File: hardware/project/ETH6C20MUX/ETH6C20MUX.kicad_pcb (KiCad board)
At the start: 4 copper layers, 160 x 100 mm, 197 parts, among them J301 5499141-4, J501 Conn_02x06_Odd_Even, J502 Conn_02x08_Odd_Even, J503 C64AC, J601 Conn_02x05, J602 Conn_02x01, K301 HE3621A0510, K302 HE3621A0510, K303 HE3621A0510, K304 HE3621A0510, K305 HE3621A0510, K306 HE3621A0510, K307 HE3621A0510, K308 HE3621A0510, K309 HE3621A0510, K310 HE3621A0510, K311 HE3621A0510, K312 HE3621A0510, K313 HE3621A0510, K314 HE3621A0510, K315 HE3621A0510, K316 HE3621A0510, K317 HE3621A0510, K318 HE3621A0510, K319 HE3621A0510, K320 HE3621A0510, K321 HE3621A0510, K322 HE3621A0510, K323 HE3621A0510, K324 HE3621A0510, K325 HE3621A0510, K326 HE3621A0510, K327 HE3621A0510, K328 HE3621A0510, K329 HE3621A0510, K330 HE3621A0510, K331 HE3621A0510, K332 HE3621A0510, K333 HE3621A0510, K334 HE3621A0510, K335 HE3621A0510, K336 HE3621A0510, K337 HE3621A0510, K338 HE3621A0510, K339 HE3621A0510, K340 HE3621A0510, K341 HE3621A0510, K342 HE3621A0510, K343 HE3621A0510, K344 HE3621A0510, K345 HE3621A0510, K346 HE3621A0510, K347 HE3621A0510, K348 HE3621A0510, K349 HE3621A0510, K350 HE3621A0510, K351 HE3621A0510, K352 HE3621A0510, K353 HE3621A0510, K354 HE3621A0510, K355 HE3621A0510, K356 HE3621A0510, K357 HE3621A0510, K358 HE3621A0510, K359 HE3621A0510, K360 HE3621A0510, K361 HE3621A0510, K362 HE3621A0510, K363 HE3621A0510, K364 HE3621A0510, K365 HE3621A0510, K366 HE3621A0510, K367 HE3621A0510, K368 HE3621A0510, K369 HE3621A0510, K370 HE3621A0510, Q401 IRFR5410, SW601 A6SN-5104, U201 LC03-3.3, U202 LAN8742A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

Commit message: Modifications in PCB main board.
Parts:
- moved R401 0.76 mm to (205.0, 132.7)
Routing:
- net GND: track 47.6 -> 45.7 mm, vias 84 -> 81
- net /Relays/PIN20: track 30.3 -> 31.4 mm
- net /Connector/RX-: track 9.42 -> 8.89 mm
- net Net-(R401-Pad2): track 3.50 -> 2.99 mm
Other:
- board text added: "01"
- board text added: "02"
- board text added: "04"
- board text added: "08"
- board text added: "16"

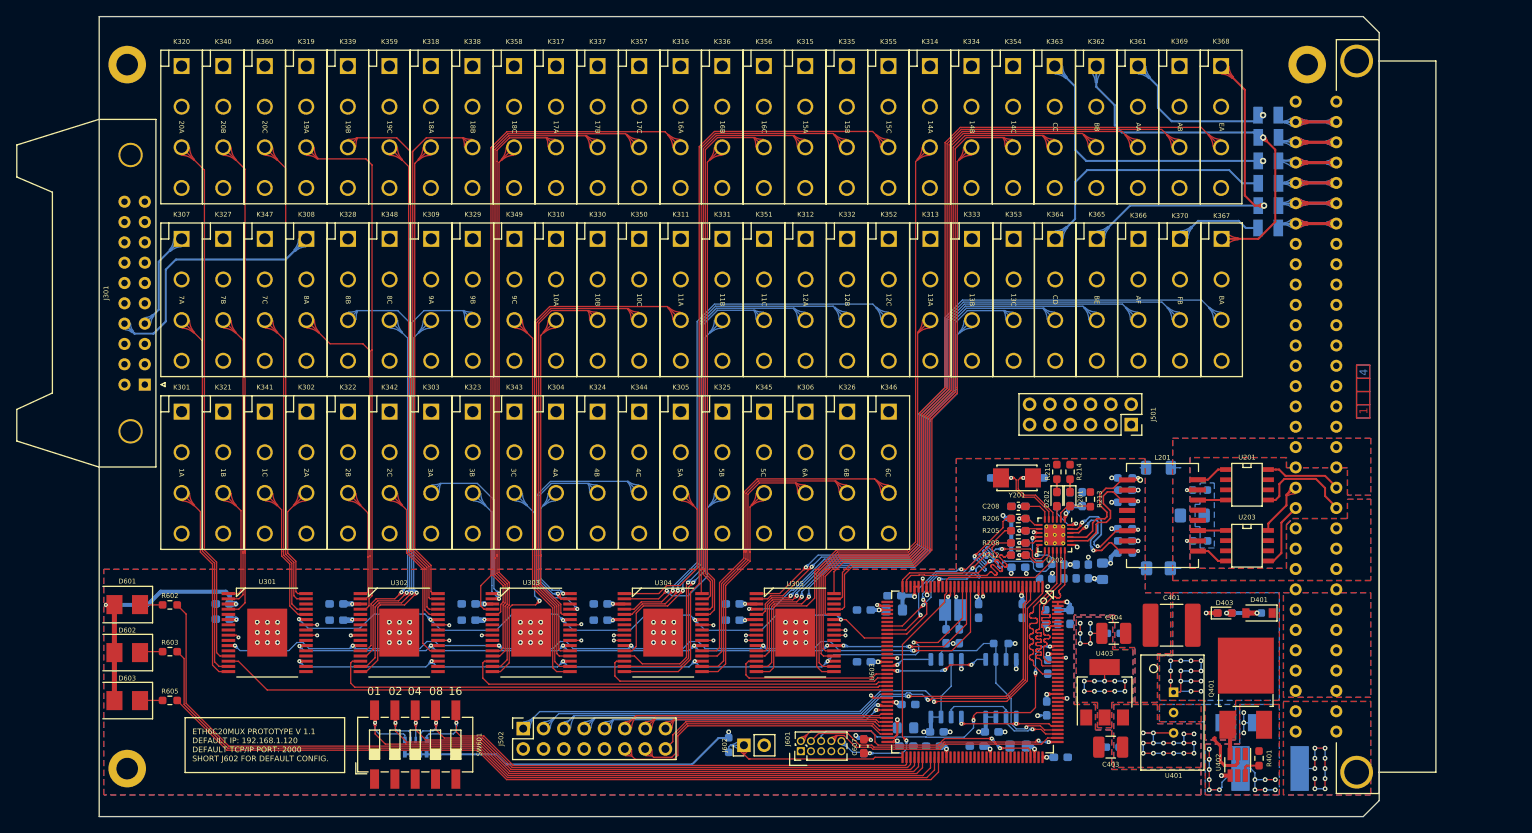
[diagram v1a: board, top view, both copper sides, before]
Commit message: PCB main and module layout.
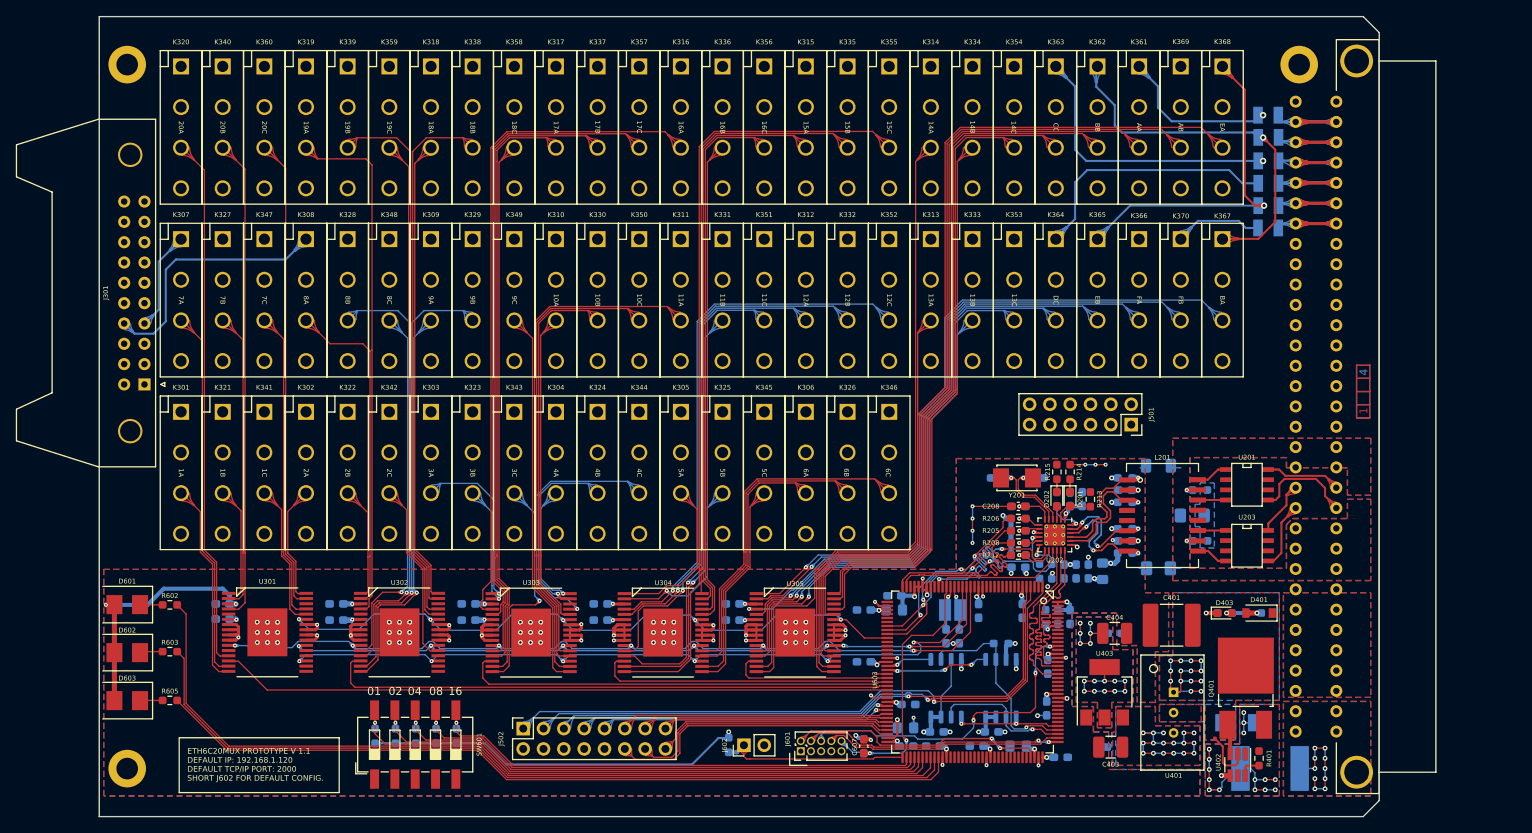
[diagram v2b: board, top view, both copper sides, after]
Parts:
- removed RN601: 10k, Resistor_SMD:R_Array_Convex_5x0603
- added R606: 10k, Resistor_SMD:R_0603_1608Metric_Pad0.98x0.95mm_HandSolder, B.Cu at (102.1, 129.9)
- added R607: 10k, Resistor_SMD:R_0603_1608Metric_Pad0.98x0.95mm_HandSolder, B.Cu at (94.5, 129.9)
- added R610: 10k, Resistor_SMD:R_0603_1608Metric_Pad0.98x0.95mm_HandSolder, B.Cu at (104.6, 129.9)
- added R611: 10k, Resistor_SMD:R_0603_1608Metric_Pad0.98x0.95mm_HandSolder, B.Cu at (97.0, 129.9)
- added R612: 10k, Resistor_SMD:R_0603_1608Metric_Pad0.98x0.95mm_HandSolder, B.Cu at (99.6, 129.9)
- moved H103 1.00 mm to (210.0, 46.0)
- moved R216 0.25 mm to (192.4, 96.1)
- moved K368 0.18 mm to (200.4, 53.8)
- moved K369 0.17 mm to (195.2, 53.8)
- moved K361 0.16 mm to (190.0, 53.8)
- moved K362 0.16 mm to (184.8, 53.8)
- moved K363 0.15 mm to (179.6, 53.8)
- moved K354 0.14 mm to (174.4, 53.8)
- moved K334 0.14 mm to (169.2, 53.8)
- moved K314 0.13 mm to (164.0, 53.8)
- moved C402 0.13 mm to (186.8, 131.3)
- moved C404 0.13 mm to (186.9, 117.1)
- moved C405 0.13 mm to (186.9, 117.1)
- moved K367 0.11 mm to (200.4, 75.4)
- moved K370 0.11 mm to (195.2, 75.4)
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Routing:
- net GND: track 45.7 -> 129.3 mm, vias 81 -> 93
- net +3V3: track 164.8 -> 174.8 mm
- net /MCU/ETH_CODE4: track 68.1 -> 63.3 mm
- net /MCU/ETH_CODE0: track 80.2 -> 75.5 mm
- net VCCQ: track 15.4 -> 19.3 mm
- net /MCU/ETH_CODE1: track 74.9 -> 71.9 mm
- net /MCU/ETH_CODE3: track 68.1 -> 65.2 mm
- net /Relays/PIN10C: track 367.6 -> 369.8 mm
- net /Ethernet/NRST: track 48.9 -> 50.5 mm
- net /MCU/ETH_CODE2: track 69.9 -> 68.5 mm
- net /Connector/A: track 77.9 -> 79.2 mm
- net /MCU/RELAY1_SI: track 97.3 -> 98.3 mm
- net +5V: track 34.1 -> 33.3 mm, vias 21 -> 22
- net Net-(C214-Pad1): track 10.9 -> 11.7 mm
- net Net-(C213-Pad1): track 10.2 -> 11.0 mm
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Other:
- board text added: "DC"
- board text added: "EB"
- board text added: "FA"
- board text removed: "AF"
- board text removed: "BE"
- board text removed: "CD"

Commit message: PCB layouts done.
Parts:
- moved K324 10.0 mm to (132.3, 97.0)
- moved K330 10.0 mm to (132.3, 75.4)
- moved K344 10.0 mm to (137.5, 97.0)
- moved K350 10.0 mm to (137.5, 75.4)
- moved K357 10.0 mm to (137.5, 53.8)
- moved C201 10.0 mm to (193.6, 109.4)
- moved C202 10.0 mm to (184.9, 108.8)
- moved C203 10.0 mm to (191.4, 100.3)
- moved C204 10.0 mm to (192.1, 109.4)
- moved C205 10.0 mm to (192.9, 100.3)
- moved C206 10.0 mm to (190.6, 109.4)
- moved C207 10.0 mm to (198.2, 105.5)
- moved C208 10.0 mm to (184.9, 101.2)
- moved C209 10.0 mm to (184.9, 101.2)
- moved C210 10.0 mm to (198.2, 99.2)
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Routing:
- net /MCU/RELAY1_~CS1: track 71.2 -> 70.6 mm
- net /MCU/RELAY1_~RST: track 86.3 -> 85.8 mm
